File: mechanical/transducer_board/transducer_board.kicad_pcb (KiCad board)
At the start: 2 copper layers, 66.6 x 66.6 mm, 63 parts, among them J1 Conn_02x17_Top_Bottom, J2 Conn_01x01, J3 Conn_01x01, U1 XL62783, U2 XL62083, U3 XL62783, U4 XL62083

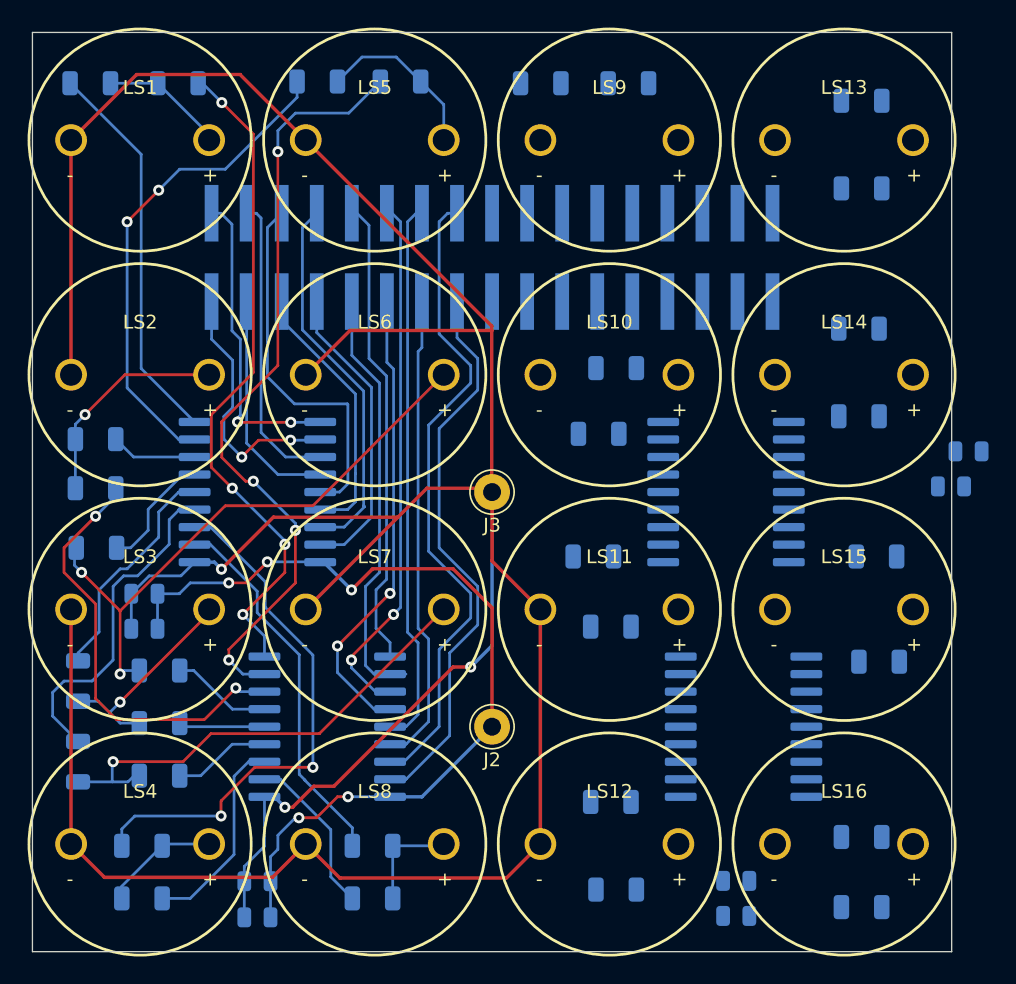
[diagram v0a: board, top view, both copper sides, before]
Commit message: Completed transducer board layout
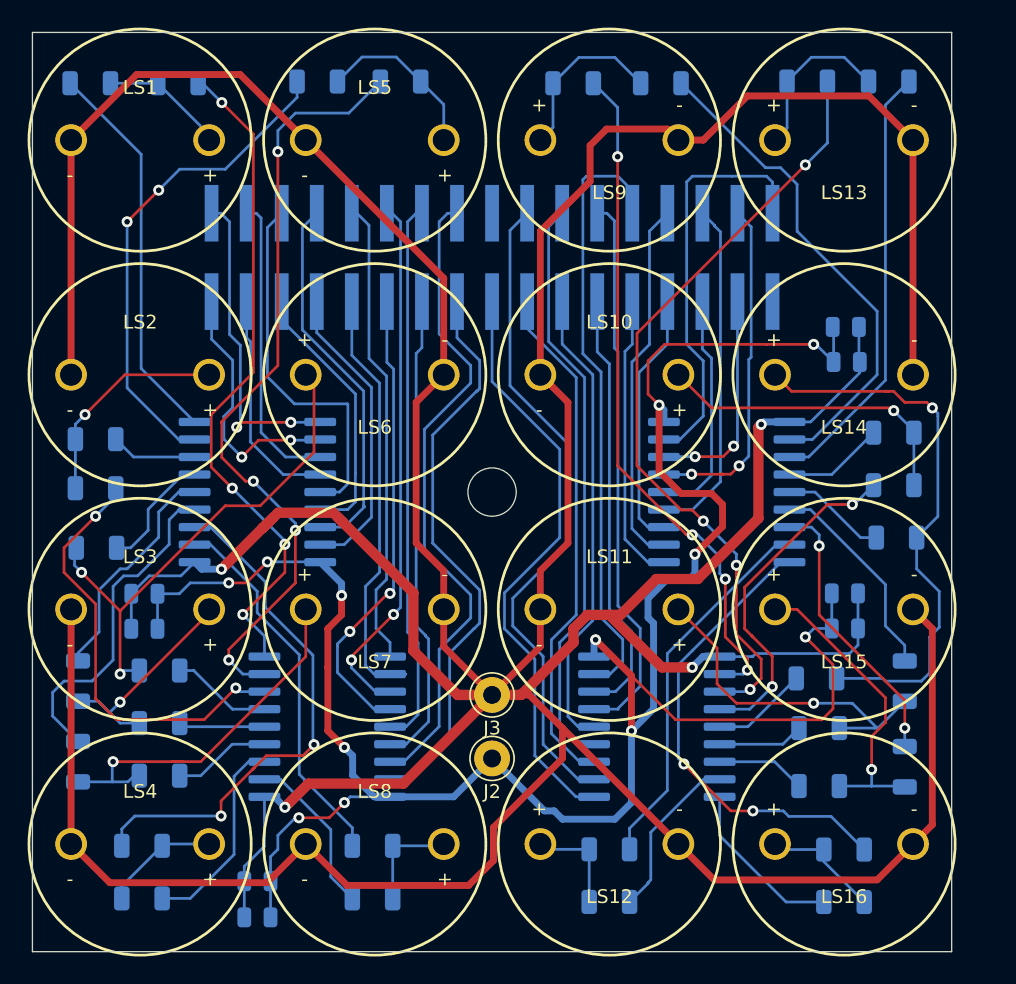
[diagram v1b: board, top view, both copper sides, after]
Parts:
- added REF**: MountingHole_3.5mm, MountingHole:MountingHole_3.5mm, F.Cu at (125.5, 125.5)
- J1: value Conn_02x17_Top_Bottom -> Conn_02x17_Odd_Even
- moved R26 25.5 mm to (149.0, 139.0), turned to 180 degrees
- moved C8 22.3 mm to (151.1, 135.4)
- moved C6 22.3 mm to (151.1, 132.8)
- moved R18 21.8 mm to (154.6, 125.0), turned to 180 degrees
- moved R23 21.7 mm to (155.4, 139.2), turned to 90 degrees
- moved R22 21.4 mm to (154.6, 121.2), turned to 180 degrees
- moved R19 20.5 mm to (149.2, 142.6), turned to 180 degrees
- moved R27 17.1 mm to (149.2, 146.8), turned to 180 degrees
- moved J3 14.7 mm to (125.5, 140.2)
- moved C7 12.7 mm to (151.1, 113.5)
- moved C5 11.8 mm to (151.2, 116.1)
- moved R30 9.20 mm to (154.8, 128.8), turned to 180 degrees
- moved R29 7.99 mm to (154.2, 95.8)
- moved R31 7.83 mm to (155.4, 145.4), turned to 90 degrees
- moved R20 7.24 mm to (134.0, 155.2)
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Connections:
- J1 pad 10: /T2- -> /T5-
- J1 pad 11: /T3- -> /T2-
- J1 pad 12: /T4- -> /T6-
- J1 pad 13: /T5- -> /T3-
- J1 pad 14: /T6- -> /T7-
- J1 pad 15: /T7- -> /T4-
- J1 pad 18: /T9+ -> /T16+
- J1 pad 19: /T10+ -> /T12+
- J1 pad 2: /T2+ -> /T5+
- J1 pad 20: /T11+ -> /T15+
- J1 pad 21: /T12+ -> /T11+
- J1 pad 22: /T13+ -> /T14+
- J1 pad 23: /T14+ -> /T10+
- J1 pad 24: /T15+ -> /T13+
- J1 pad 25: /T16+ -> /T9+
- J1 pad 26: /T9- -> /T16-
- J1 pad 27: /T10- -> /T12-
- J1 pad 28: /T11- -> /T15-
- J1 pad 29: /T12- -> /T11-
- J1 pad 3: /T3+ -> /T2+
- J1 pad 30: /T13- -> /T14-
- J1 pad 31: /T14- -> /T10-
- J1 pad 32: /T15- -> /T13-
- J1 pad 33: /T16- -> /T9-
- J1 pad 4: /T4+ -> /T6+
- J1 pad 5: /T5+ -> /T3+
- J1 pad 6: /T6+ -> /T7+
- J1 pad 7: /T7+ -> /T4+
- U1 pad 2: /T2+ -> /T5+
- U1 pad 3: /T3+ -> /T2+
- U1 pad 4: /T4+ -> /T6+
- U1 pad 5: /T5+ -> /T3+
- U1 pad 6: /T6+ -> /T7+
- U1 pad 7: /T7+ -> /T4+
- U2 pad 2: /T2- -> /T5-
- U2 pad 3: /T3- -> /T2-
- U2 pad 4: /T4- -> /T6-
- U2 pad 5: /T5- -> /T3-
- U2 pad 6: /T6- -> /T7-
- U2 pad 7: /T7- -> /T4-
- U3 pad 1: /T9+ -> /T16+
- U3 pad 11: Net-(R28-Pad2) -> Net-(R17-Pad2)
- U3 pad 12: Net-(R20-Pad2) -> Net-(R25-Pad2)
- U3 pad 13: Net-(R27-Pad2) -> Net-(R18-Pad2)
- U3 pad 14: Net-(R19-Pad2) -> Net-(R26-Pad2)
- U3 pad 15: Net-(R26-Pad2) -> Net-(R19-Pad2)
- U3 pad 16: Net-(R18-Pad2) -> Net-(R27-Pad2)
- U3 pad 17: Net-(R25-Pad2) -> Net-(R20-Pad2)
- U3 pad 18: Net-(R17-Pad2) -> Net-(R28-Pad2)
- U3 pad 2: /T10+ -> /T12+
- U3 pad 3: /T11+ -> /T15+
- U3 pad 4: /T12+ -> /T11+
- U3 pad 5: /T13+ -> /T14+
- U3 pad 6: /T14+ -> /T10+
- U3 pad 7: /T15+ -> /T13+
- U3 pad 8: /T16+ -> /T9+
- U4 pad 1: /T9- -> /T16-
- U4 pad 11: Net-(R32-Pad2) -> Net-(R21-Pad2)
- U4 pad 12: Net-(R24-Pad2) -> Net-(R29-Pad2)
- U4 pad 13: Net-(R31-Pad2) -> Net-(R22-Pad2)
- U4 pad 14: Net-(R23-Pad2) -> Net-(R30-Pad2)
- U4 pad 15: Net-(R30-Pad2) -> Net-(R23-Pad2)
- U4 pad 16: Net-(R22-Pad2) -> Net-(R31-Pad2)
- U4 pad 17: Net-(R29-Pad2) -> Net-(R24-Pad2)
- U4 pad 18: Net-(R21-Pad2) -> Net-(R32-Pad2)
- U4 pad 2: /T10- -> /T12-
- U4 pad 3: /T11- -> /T15-
- U4 pad 4: /T12- -> /T11-
- U4 pad 5: /T13- -> /T14-
- U4 pad 6: /T14- -> /T10-
- U4 pad 7: /T15- -> /T13-
- U4 pad 8: /T16- -> /T9-
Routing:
- net GND: track 249.5 -> 431.5 mm, vias 3 -> 4
- net VCC: track 63.9 -> 167.1 mm, vias 5 -> 12
- net Net-(R25-Pad2): track 0.00 -> 56.6 mm, vias 0 -> 4
- net Net-(R17-Pad2): track 0.00 -> 49.7 mm, vias 0 -> 4
- net /T12+: track 0.00 -> 48.0 mm
- net /T9+: track 0.00 -> 44.3 mm
- net /T16+: track 0.00 -> 43.0 mm
- net /T11+: track 0.00 -> 42.4 mm
- net Net-(LS14-Pad1): track 0.00 -> 40.6 mm, vias 0 -> 1
- net /T10+: track 0.00 -> 40.0 mm
- net /T15+: track 0.00 -> 37.5 mm
- net Net-(R21-Pad2): track 0.00 -> 35.9 mm
- net Net-(R32-Pad2): track 0.00 -> 34.1 mm, vias 0 -> 2
- net /T14+: track 0.00 -> 33.9 mm
- net Net-(R29-Pad2): track 0.00 -> 31.6 mm
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
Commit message: Transducer board update
Flipped front and back, added ground plane, and thickened bypass cap traces
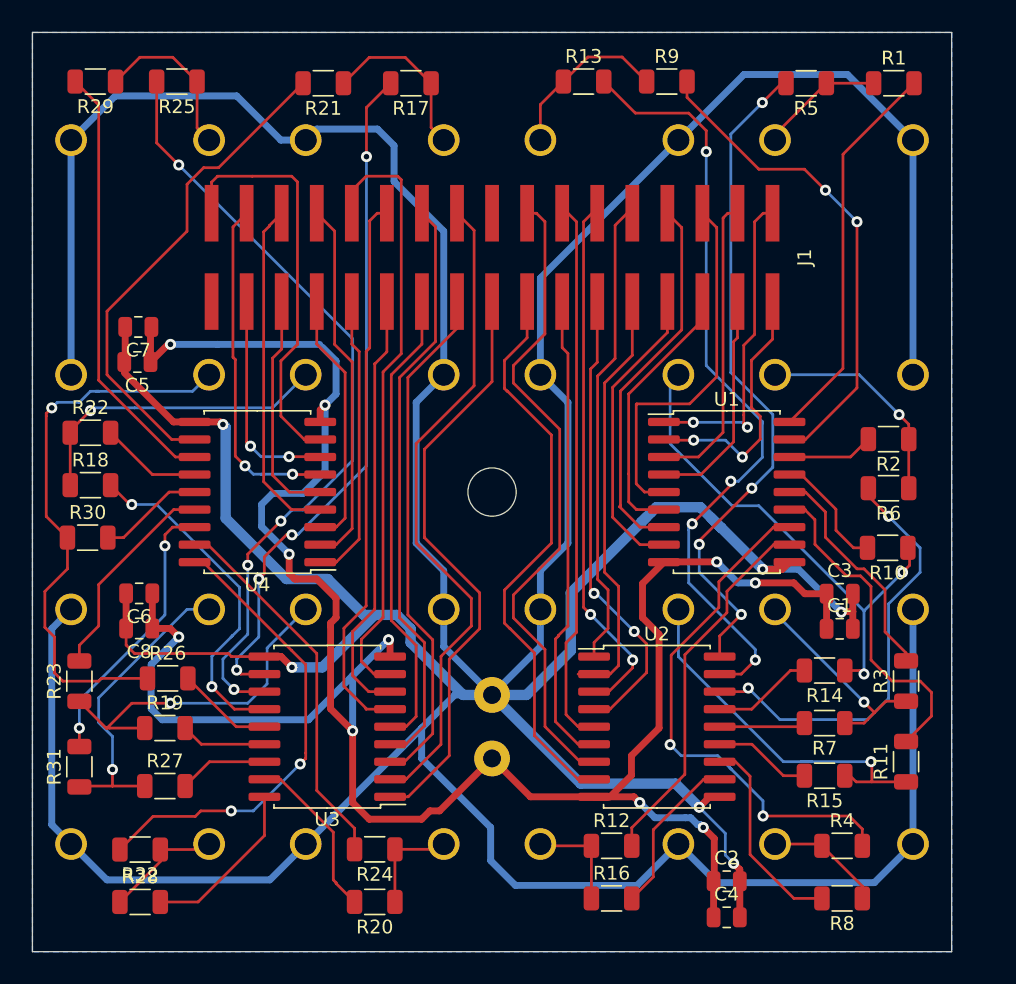
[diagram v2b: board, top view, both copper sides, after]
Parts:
- C1, C2, C3, C4, C5, C6, C7, C8, J1, R1, R10, R11, R12, R13, R14, R15, R16, R17, R18, R19, R2, R20, R21, R22, R23, R24, R25, R26, R27, R28, R29, R3, R30, R31, R32, R4, R5, R6, R7, R8, R9, U1, U2, U3, U4: moved to F.Cu
- J2, J3, LS1, LS10, LS11, LS12, LS13, LS14, LS15, LS16, LS2, LS3, LS4, LS5, LS6, LS7, LS8, LS9, REF**: moved to B.Cu
- moved R11 60.0 mm to (155.5, 145.0)
- moved R3 60.0 mm to (155.5, 139.2)
- moved R23 59.8 mm to (95.6, 139.2)
- moved R31 59.8 mm to (95.6, 145.4)
- moved R30 58.6 mm to (96.2, 128.8), turned to 0 degrees
- moved R1 58.2 mm to (154.6, 95.9), turned to 0 degrees
- moved R18 58.2 mm to (96.4, 125.0), turned to 0 degrees
- moved R22 58.2 mm to (96.4, 121.2), turned to 0 degrees
- moved R29 57.5 mm to (96.8, 95.8), turned to 180 degrees
- moved R2 57.5 mm to (154.2, 121.7), turned to 180 degrees
- moved R6 57.5 mm to (154.2, 125.2), turned to 180 degrees
- moved R10 57.3 mm to (154.2, 129.5), turned to 180 degrees
- moved C5 51.4 mm to (99.8, 116.1), turned to 180 degrees
- moved C7 51.3 mm to (99.9, 113.5), turned to 180 degrees
- moved C6 51.1 mm to (99.9, 132.8), turned to 180 degrees
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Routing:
- net GND: track 431.5 -> 434.0 mm, vias 4 -> 6
- net VCC: track 167.1 -> 167.5 mm, vias 12 -> 10
- added copper zone on B.Cu, net GND

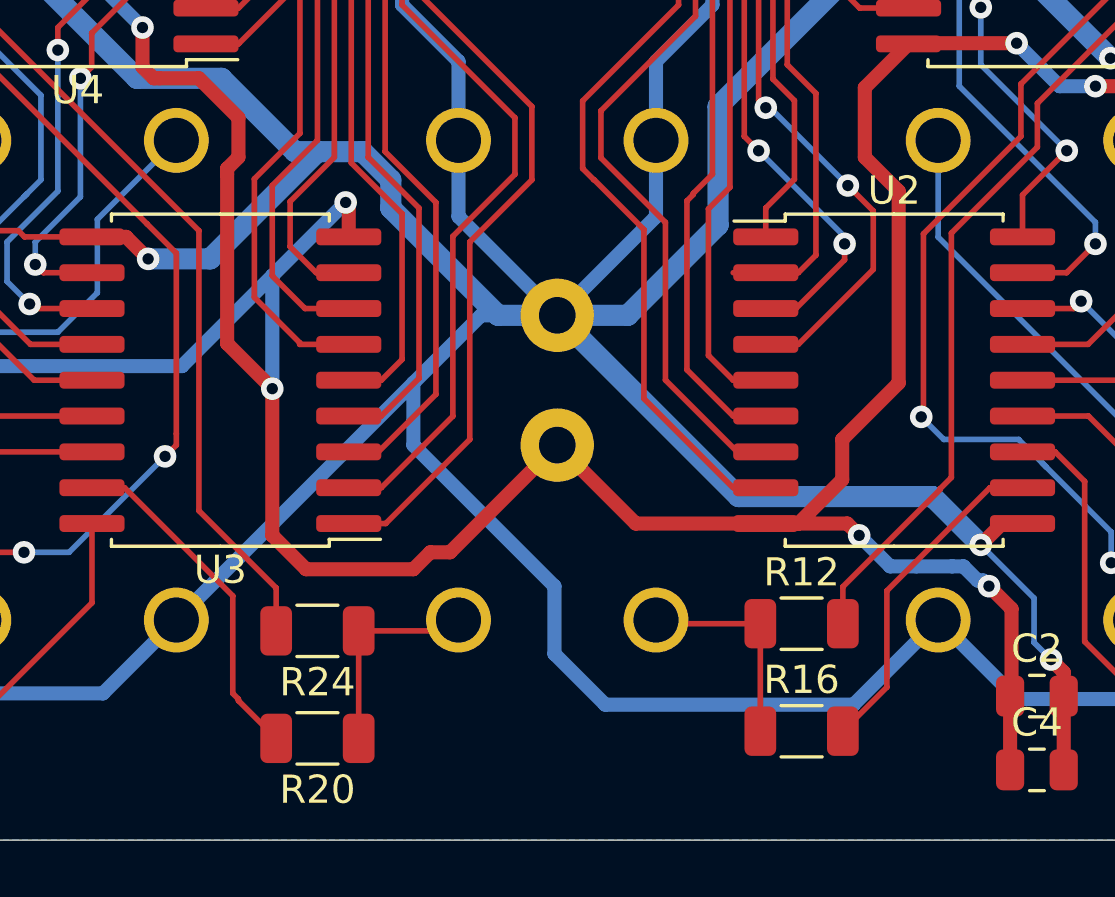
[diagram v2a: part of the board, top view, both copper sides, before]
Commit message: Transducers are driven with a bipolar waveform
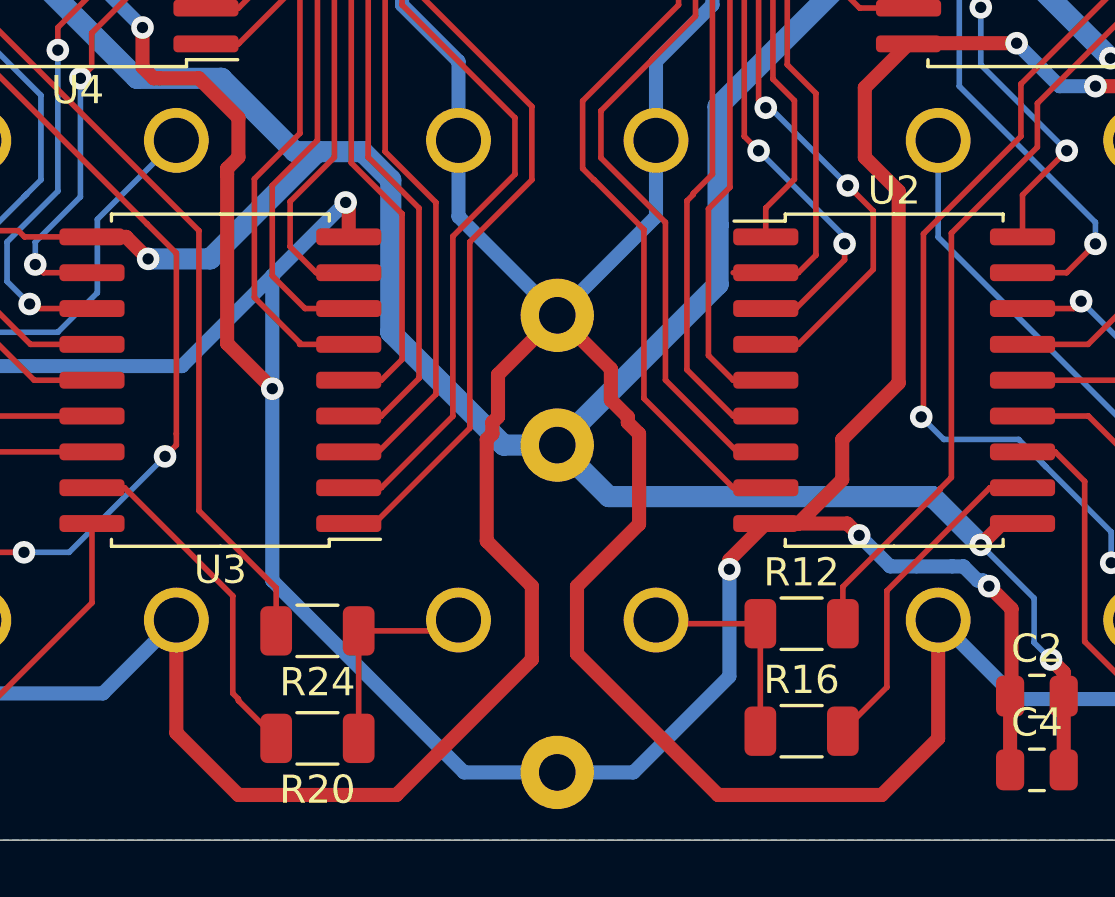
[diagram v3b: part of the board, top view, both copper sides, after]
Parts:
- added J4: Conn_01x01, Connector_Pin:Pin_D1.3mm_L11.0mm, B.Cu at (125.5, 140.2)
- moved J2 11.6 mm to (125.5, 156.4)
- moved J3 4.60 mm to (125.5, 144.8)
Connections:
- LS1 pad 2: GND -> /VMID
- LS10 pad 2: GND -> /VMID
- LS11 pad 2: GND -> /VMID
- LS12 pad 2: GND -> /VMID
- LS13 pad 2: GND -> /VMID
- LS14 pad 2: GND -> /VMID
- LS15 pad 2: GND -> /VMID
- LS16 pad 2: GND -> /VMID
- LS2 pad 2: GND -> /VMID
- LS3 pad 2: GND -> /VMID
- LS4 pad 2: GND -> /VMID
- LS5 pad 2: GND -> /VMID
- LS6 pad 2: GND -> /VMID
- LS7 pad 2: GND -> /VMID
- LS8 pad 2: GND -> /VMID
- LS9 pad 2: GND -> /VMID
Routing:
- net /VMID: track 0.00 -> 314.7 mm
- net GND: track 434.0 -> 147.2 mm
- net VCC: track 167.5 -> 173.9 mm, vias 10 -> 11
